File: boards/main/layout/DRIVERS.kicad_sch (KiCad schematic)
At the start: 31 parts, among them IC5 L6205D013TR, IC6 STSPIN958TR, M1 B02B-PASK(LF)(SN), M2 B02B-PASK(LF)(SN), M3 B02B-PASK(LF)(SN)

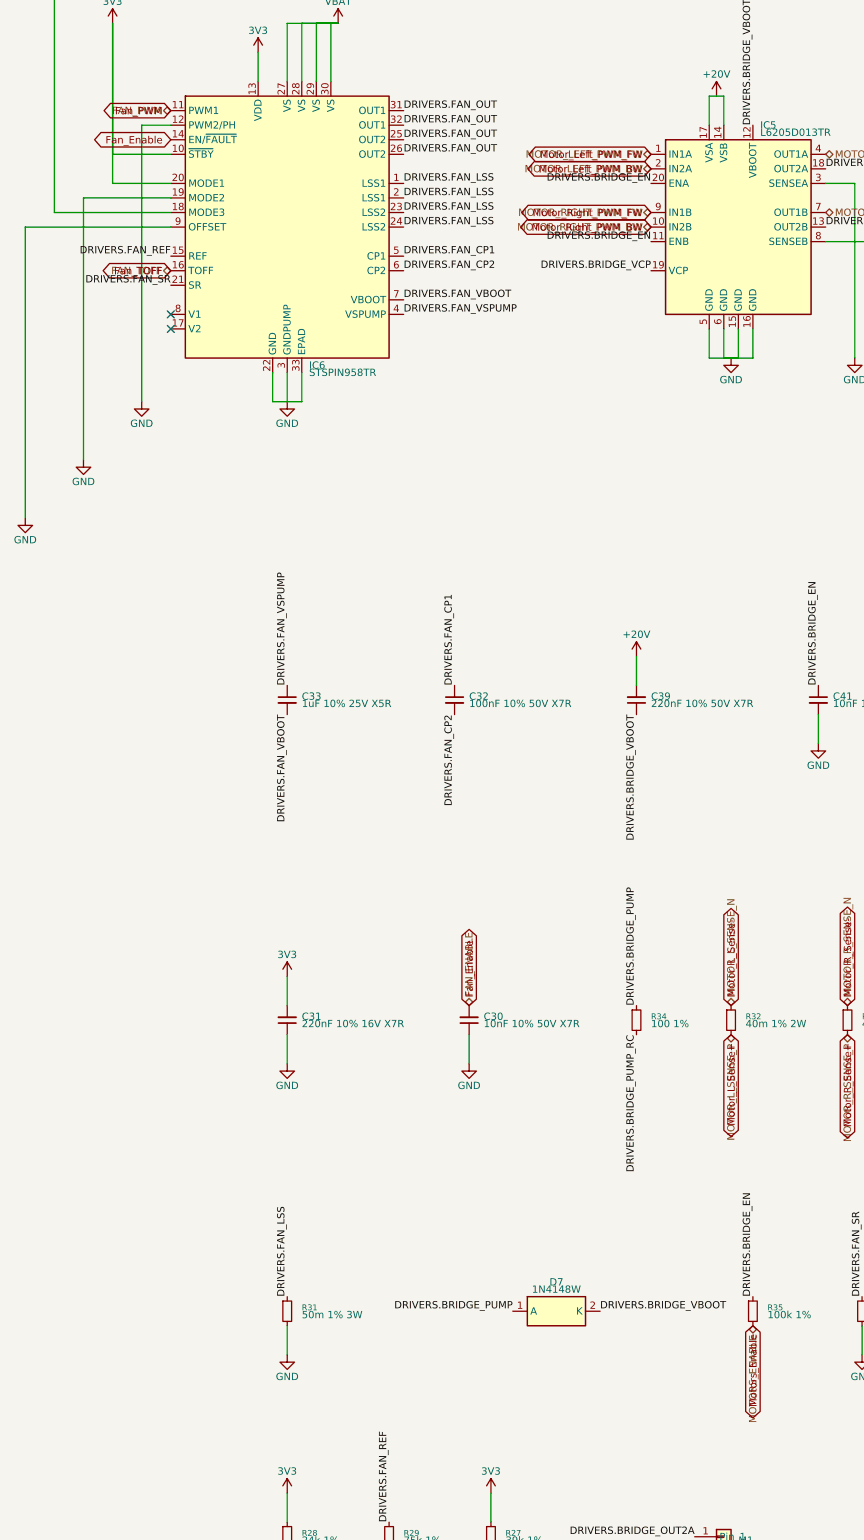
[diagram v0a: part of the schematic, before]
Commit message: 🏷️ Name the main board's module ports after their nets
A sheet pin and its hierarchical label take the module's port name and the root's label the net
name; KiCad's ERC flagged the 33 nets whose two names differed only in case (similar_labels).
GND_BAT becomes a ground port of REGULATORS, so the root shows a power symbol at its sheet pin
instead of a label nothing else joined (label_dangling).
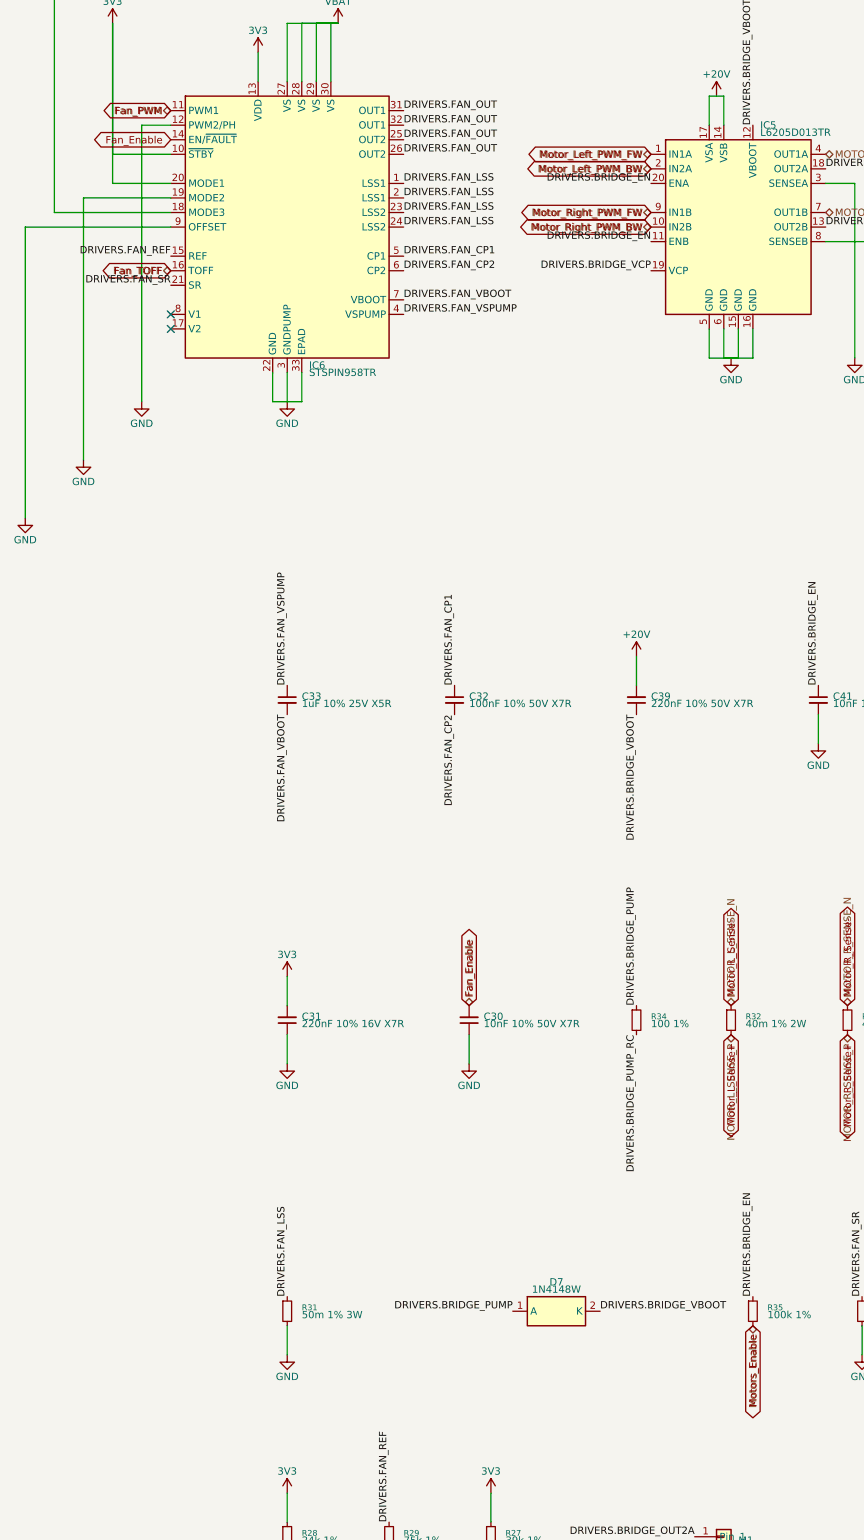
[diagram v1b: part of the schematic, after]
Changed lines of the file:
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@@
 		)
 	)
-	(hierarchical_label "MOTOR_L_SENSE_P"
+	(hierarchical_label "Motor_Left_PWM_FW"
 		(shape bidirectional)
-		(at 214.63 247.65 270)
+		(at 200.66 93.98 180)
 		(effects
 			(font
@@
 		)
 	)
-	(hierarchical_label "MOTOR_RIGHT_PWM_FW"
+	(hierarchical_label "MOTOR_L_SENSE_P"
 		(shape bidirectional)
-		(at 200.66 104.14 180)
+		(at 214.63 247.65 270)
 		(effects
 			(font
@@
 		)
 	)
-	(hierarchical_label "MOTOR_LEFT_PWM_BW"
+	(hierarchical_label "Motors_Enable"
 		(shape bidirectional)
-		(at 200.66 96.52 180)
+		(at 218.44 298.45 270)
 		(effects
 			(font
@@
 		)
 	)
-	(hierarchical_label "FAN_TOFF"
+	(hierarchical_label "Fan_PWM"
 		(shape bidirectional)
-		(at 116.84 114.3 180)
+		(at 116.84 86.36 180)
 		(effects
 			(font
@@
 		)
 	)
-	(hierarchical_label "MOTOR_R_SENSE_N"
+	(hierarchical_label "Fan_Enable"
 		(shape bidirectional)
-		(at 262.89 337.82 180)
+		(at 168.91 242.57 90)
 		(effects
 			(font
 				(size 1.27 1.27)
 			)
-			(justify right)
+			(justify left)
 		)
 	)
-	(hierarchical_label "FAN_PWM"
+	(hierarchical_label "MOTOR_R_SENSE_N"
 		(shape bidirectional)
-		(at 116.84 86.36 180)
+		(at 262.89 337.82 180)
 		(effects
 			(font
@@
 		)
 	)
-	(hierarchical_label "MOTORS_ENABLE"
-		(shape bidirectional)
-		(at 218.44 298.45 270)
-		(effects
-			(font
-				(size 1.27 1.27)
-			)
-			(justify right)
-		)
-	)
 	(hierarchical_label "MOTOR_R_SENSE_P"
 		(shape bidirectional)
@@
 		)
 	)
-	(hierarchical_label "FAN_ENABLE"
+	(hierarchical_label "Fan_TOFF"
 		(shape bidirectional)
-		(at 168.91 242.57 90)
+		(at 116.84 114.3 180)
 		(effects
 			(font
 				(size 1.27 1.27)
 			)
-			(justify left)
+			(justify right)
 		)
 	)
@@
 		)
 	)
-	(hierarchical_label "MOTOR_LEFT_PWM_FW"
+	(hierarchical_label "Motor_Right_PWM_FW"
 		(shape bidirectional)
-		(at 200.66 93.98 180)
+		(at 200.66 104.14 180)
 		(effects
 			(font
@@
 		)
 	)
-	(hierarchical_label "MOTOR_RIGHT_PWM_BW"
+	(hierarchical_label "Motor_Left_PWM_BW"
+		(shape bidirectional)
+		(at 200.66 96.52 180)
+		(effects
+			(font
+				(size 1.27 1.27)
+			)
+			(justify right)
+		)
+	)
+	(hierarchical_label "Motor_Right_PWM_BW"
 		(shape bidirectional)
 		(at 200.66 106.68 180)

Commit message: ✨ Place the schematics from per-sheet placement files
micras-pcb sch redraws each sheet pcb apply writes from
boards/<board>/schematic/<sheet>.toml: parts, wires, labels, power
symbols, titled frames, paper and title block, the root's sheet
symbols, and a ports column for the module sheets' extra labels. It
fails unless KiCad's netlist of the placed schematic equals pcb's.
make gen runs it after pcb apply; make check's sch gate fails on a part
without a placement, and tests/test_placement.py on any overlap.

The encoder and Bluetooth sheets are placed; the main board's DRIVERS
sheet is drafted.
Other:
- note added: "Fan driver: STSPIN958, current limit through R31"
- note added: "Motor bridge: L6205, current sense through R32 and R33"
- note added: "Sheet ports"
- title: (none) -> Motor and fan drivers
- moved on the sheet: C30, C31, C32, C33, C34, C35, C36, C37, C38, C39, C40, C41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
